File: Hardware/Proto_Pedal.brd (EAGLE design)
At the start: 85.1 x 110.5 mm, 124 parts, among them Q1 2.5A/30V

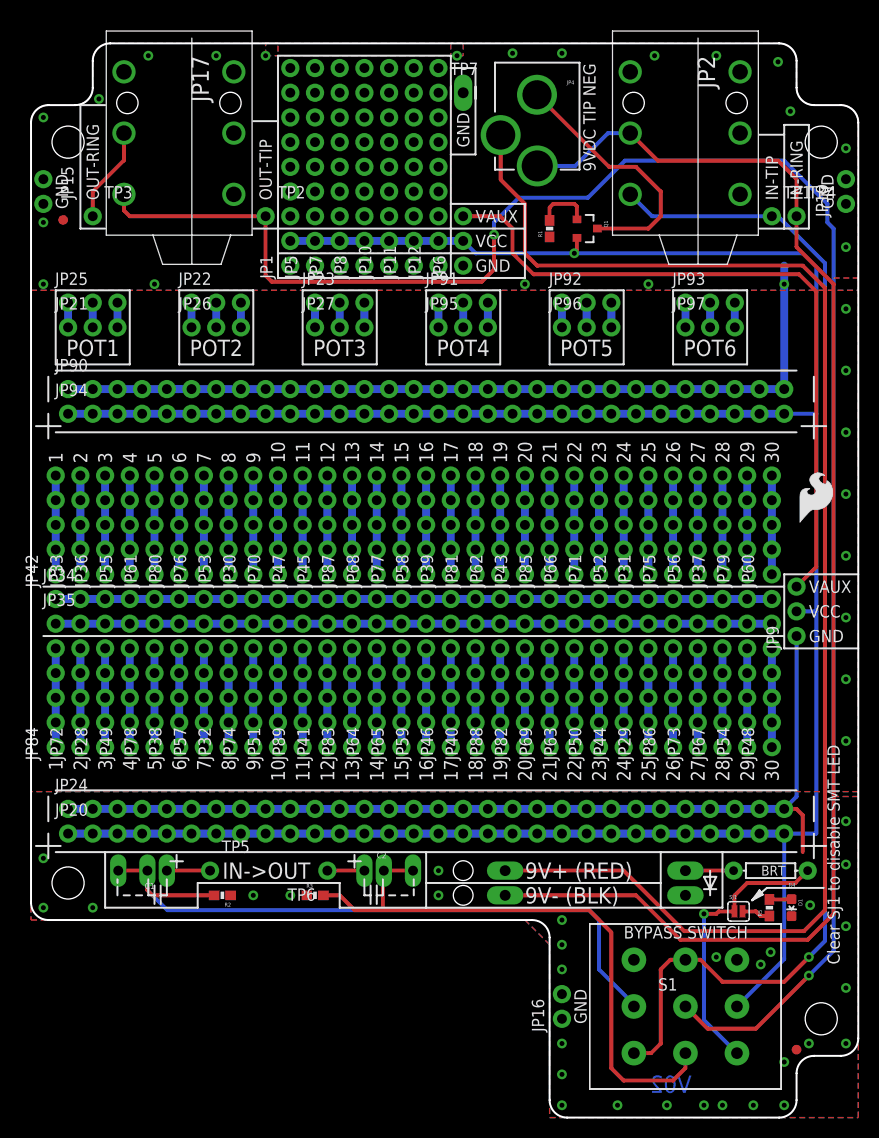
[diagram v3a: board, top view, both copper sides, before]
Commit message: Tweaks from checklist.
- and + signs on rails are a bit smaller.
+'s next to C1 and C2 were overlapping bare copper.
Version bumped to V03.
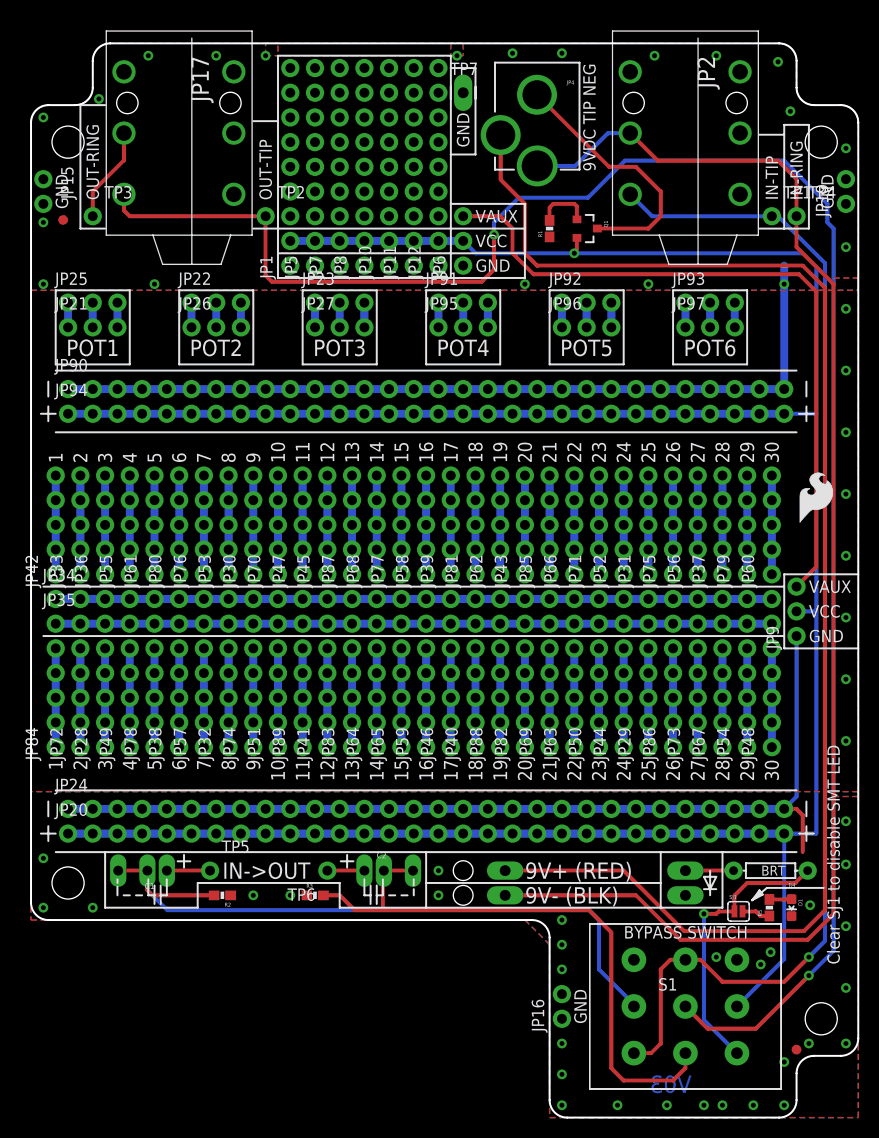
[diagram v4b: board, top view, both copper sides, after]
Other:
- board text added: "V03"
- board text removed: "V02"
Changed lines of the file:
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@@
 <setting verticaltext="up"/>
 </settings>
-<grid distance="0.05" unitdist="inch" unit="inch" style="lines" multiple="1" display="yes" altdistance="0.005" altunitdist="inch" altunit="inch"/>
+<grid distance="0.1" unitdist="inch" unit="inch" style="lines" multiple="1" display="yes" altdistance="0.01" altunitdist="inch" altunit="inch"/>
 <layers>
 <layer number="1" name="Top" color="4" fill="1" visible="yes" active="yes"/>
@@
 <layer number="27" name="tValues" color="7" fill="1" visible="no" active="yes"/>
 <layer number="28" name="bValues" color="7" fill="1" visible="no" active="yes"/>
-<layer number="29" name="tStop" color="7" fill="3" visible="no" active="yes"/>
-<layer number="30" name="bStop" color="7" fill="6" visible="no" active="yes"/>
+<layer number="29" name="tStop" color="7" fill="3" visible="yes" active="yes"/>
+<layer number="30" name="bStop" color="7" fill="6" visible="yes" active="yes"/>
 <layer number="31" name="tCream" color="7" fill="4" visible="no" active="yes"/>
 <layer number="32" name="bCream" color="7" fill="5" visible="no" active="yes"/>
@@
 <wire x1="44.45" y1="17.78" x2="50.8" y2="17.78" width="0.2032" layer="51"/>
 <wire x1="44.45" y1="17.78" x2="44.45" y2="0" width="0.2032" layer="51"/>
-<wire x1="0.508" y1="71.12" x2="1.778" y2="71.12" width="0.2032" layer="21"/>
-<wire x1="1.778" y1="71.12" x2="1.778" y2="69.85" width="0.2032" layer="21"/>
-<wire x1="1.778" y1="72.39" x2="1.778" y2="71.12" width="0.2032" layer="21"/>
-<wire x1="1.778" y1="73.66" x2="1.778" y2="76.2" width="0.2032" layer="21"/>
-<wire x1="0.508" y1="71.12" x2="1.778" y2="71.12" width="0.2032" layer="22"/>
-<wire x1="3.048" y1="71.12" x2="1.778" y2="71.12" width="0.2032" layer="22"/>
-<wire x1="1.778" y1="71.12" x2="1.778" y2="69.85" width="0.2032" layer="22"/>
-<wire x1="1.778" y1="72.39" x2="1.778" y2="71.12" width="0.2032" layer="22"/>
-<wire x1="1.778" y1="73.66" x2="1.778" y2="76.2" width="0.2032" layer="22"/>
-<wire x1="0.508" y1="27.94" x2="1.778" y2="27.94" width="0.2032" layer="21"/>
-<wire x1="3.048" y1="27.94" x2="1.778" y2="27.94" width="0.2032" layer="21"/>
-<wire x1="1.778" y1="27.94" x2="1.778" y2="26.67" width="0.2032" layer="21"/>
-<wire x1="1.778" y1="29.21" x2="1.778" y2="27.94" width="0.2032" layer="21"/>
-<wire x1="1.778" y1="30.48" x2="1.778" y2="33.02" width="0.2032" layer="21"/>
-<wire x1="0.508" y1="27.94" x2="1.778" y2="27.94" width="0.2032" layer="22"/>
-<wire x1="3.048" y1="27.94" x2="1.778" y2="27.94" width="0.2032" layer="22"/>
-<wire x1="1.778" y1="27.94" x2="1.778" y2="26.67" width="0.2032" layer="22"/>
-<wire x1="1.778" y1="29.21" x2="1.778" y2="27.94" width="0.2032" layer="22"/>
-<wire x1="1.778" y1="30.48" x2="1.778" y2="33.02" width="0.2032" layer="22"/>
-<wire x1="79.248" y1="71.12" x2="80.518" y2="71.12" width="0.2032" layer="21"/>
-<wire x1="81.788" y1="71.12" x2="80.518" y2="71.12" width="0.2032" layer="21"/>
-<wire x1="80.518" y1="71.12" x2="80.518" y2="69.85" width="0.2032" layer="21"/>
-<wire x1="80.518" y1="72.39" x2="80.518" y2="71.12" width="0.2032" layer="21"/>
-<wire x1="80.518" y1="73.66" x2="80.518" y2="76.2" width="0.2032" layer="21"/>
-<wire x1="79.248" y1="71.12" x2="80.518" y2="71.12" width="0.2032" layer="22"/>
-<wire x1="81.788" y1="71.12" x2="80.518" y2="71.12" width="0.2032" layer="22"/>
-<wire x1="80.518" y1="71.12" x2="80.518" y2="69.85" width="0.2032" layer="22"/>
-<wire x1="80.518" y1="72.39" x2="80.518" y2="71.12" width="0.2032" layer="22"/>
-<wire x1="80.518" y1="73.66" x2="80.518" y2="76.2" width="0.2032" layer="22"/>
-<wire x1="79.248" y1="27.94" x2="80.518" y2="27.94" width="0.2032" layer="21"/>
-<wire x1="81.788" y1="27.94" x2="80.518" y2="27.94" width="0.2032" layer="21"/>
-<wire x1="80.518" y1="27.94" x2="80.518" y2="26.67" width="0.2032" layer="21"/>
-<wire x1="80.518" y1="29.21" x2="80.518" y2="27.94" width="0.2032" layer="21"/>
-<wire x1="80.518" y1="30.48" x2="80.518" y2="33.02" width="0.2032" layer="21"/>
-<wire x1="79.248" y1="27.94" x2="80.518" y2="27.94" width="0.2032" layer="22"/>
-<wire x1="81.788" y1="27.94" x2="80.518" y2="27.94" width="0.2032" layer="22"/>
-<wire x1="80.518" y1="27.94" x2="80.518" y2="26.67" width="0.2032" layer="22"/>
-<wire x1="80.518" y1="29.21" x2="80.518" y2="27.94" width="0.2032" layer="22"/>
-<wire x1="80.518" y1="30.48" x2="80.518" y2="33.02" width="0.2032" layer="22"/>
 <text x="50.8" y="25.4" size="1.6764" layer="21" font="vector" ratio="15" align="center-left">9V+ (RED)</text>
 <text x="50.8" y="22.86" size="1.6764" layer="21" font="vector" ratio="15" align="center-left">9V- (BLK)</text>
@@
 <text x="69.85" y="80.01" size="1.6764" layer="21" font="vector" ratio="15" align="top-center">POT6</text>
 <wire x1="78.74" y1="70.485" x2="2.54" y2="70.485" width="0.2032" layer="21"/>
-<wire x1="1.778" y1="71.12" x2="3.048" y2="71.12" width="0.2032" layer="21"/>
 <wire x1="78.74" y1="33.655" x2="2.54" y2="33.655" width="0.2032" layer="21"/>
 <wire x1="78.74" y1="27.305" x2="71.12" y2="27.305" width="0.2032" layer="21"/>
@@
 <wire x1="39.37" y1="23.495" x2="39.37" y2="22.86" width="0.2032" layer="21"/>
 <wire x1="39.37" y1="24.511" x2="39.37" y2="23.876" width="0.2032" layer="21"/>
-<wire x1="33.928" y1="26.362" x2="32.62" y2="26.362" width="0.2032" layer="21"/>
-<wire x1="33.274" y1="27.016" x2="33.274" y2="25.708" width="0.2032" layer="21"/>
+<wire x1="33.166" y1="26.362" x2="31.858" y2="26.362" width="0.2032" layer="21"/>
+<wire x1="32.512" y1="27.016" x2="32.512" y2="25.708" width="0.2032" layer="21"/>
 <wire x1="40.64" y1="27.305" x2="40.64" y2="24.13" width="0.2032" layer="22"/>
 <wire x1="40.64" y1="21.59" x2="31.75" y2="21.59" width="0.2032" layer="22"/>
@@
 <wire x1="8.89" y1="23.749" x2="8.89" y2="22.86" width="0.2032" layer="22"/>
 <wire x1="8.89" y1="24.511" x2="8.89" y2="24.13" width="0.2032" layer="22"/>
-<wire x1="32.62" y1="26.362" x2="33.928" y2="26.362" width="0.2032" layer="22"/>
-<wire x1="33.274" y1="27.016" x2="33.274" y2="25.708" width="0.2032" layer="22"/>
+<wire x1="31.858" y1="26.362" x2="33.166" y2="26.362" width="0.2032" layer="22"/>
+<wire x1="32.512" y1="27.016" x2="32.512" y2="25.708" width="0.2032" layer="22"/>
 <text x="19.177" y="25.4" size="1.6764" layer="22" font="vector" ratio="15" rot="MR180" align="center-left">OUT&lt;-IN</text>
-<text x="67.945" y="2.54" size="1.778" layer="16" font="vector" ratio="15" rot="MR0">V02</text>
+<text x="67.945" y="2.54" size="1.778" layer="16" font="vector" ratio="15" rot="MR0">V03</text>
 <dimension x1="0" y1="0" x2="0" y2="110.49" x3="-16.51" y3="55.245" textsize="1.778" textratio="15" layer="47" unit="inch"/>
 <text x="11.43" y="-19.05" size="2.54" layer="47" ratio="15">All Dimensions in inches
@@
 <wire x1="80.01" y1="91.44" x2="80.01" y2="102.108" width="0.2032" layer="21"/>
 <text x="78.74" y="94.361" size="1.27" layer="22" font="vector" ratio="15" rot="MR90" align="center-left">IN-RING</text>
-<wire x1="15.628" y1="26.362" x2="14.32" y2="26.362" width="0.2032" layer="21"/>
-<wire x1="14.974" y1="27.016" x2="14.974" y2="25.708" width="0.2032" layer="21"/>
-<wire x1="14.32" y1="26.362" x2="15.628" y2="26.362" width="0.2032" layer="22"/>
-<wire x1="14.974" y1="27.016" x2="14.974" y2="25.708" width="0.2032" layer="22"/>
+<wire x1="16.39" y1="26.362" x2="15.082" y2="26.362" width="0.2032" layer="21"/>
+<wire x1="15.736" y1="27.016" x2="15.736" y2="25.708" width="0.2032" layer="21"/>
+<wire x1="15.082" y1="26.362" x2="16.39" y2="26.362" width="0.2032" layer="22"/>
+<wire x1="15.736" y1="27.016" x2="15.736" y2="25.708" width="0.2032" layer="22"/>
 <dimension x1="0" y1="110.49" x2="52.07" y2="110.49" x3="26.035" y3="138.684" textsize="2.54" textratio="15" layer="47" unit="inch"/>
 <text x="2.54" y="95.25" size="1.27" layer="22" font="vector" ratio="15" rot="MR270" align="top-center">GND</text>
@@
 <wire x1="74.7268" y1="22.987" x2="74.93" y2="23.1648" width="0.254" layer="21"/>
 <wire x1="74.93" y1="23.1648" x2="75.0316" y2="22.987" width="0.254" layer="21"/>
+<wire x1="79.756" y1="32.512" x2="79.756" y2="30.988" width="0.2032" layer="21"/>
+<wire x1="79.756" y1="29.972" x2="79.756" y2="28.448" width="0.2032" layer="21"/>
+<wire x1="78.994" y1="29.21" x2="80.518" y2="29.21" width="0.2032" layer="21"/>
+<wire x1="79.756" y1="32.512" x2="79.756" y2="30.988" width="0.2032" layer="22"/>
+<wire x1="79.756" y1="29.972" x2="79.756" y2="28.448" width="0.2032" layer="22"/>
+<wire x1="80.518" y1="29.21" x2="78.994" y2="29.21" width="0.2032" layer="22"/>
+<wire x1="1.778" y1="32.512" x2="1.778" y2="30.988" width="0.2032" layer="21"/>
+<wire x1="1.778" y1="29.972" x2="1.778" y2="28.448" width="0.2032" layer="21"/>
+<wire x1="1.016" y1="29.21" x2="2.54" y2="29.21" width="0.2032" layer="21"/>
+<wire x1="1.778" y1="32.512" x2="1.778" y2="30.988" width="0.2032" layer="22"/>
+<wire x1="1.778" y1="29.972" x2="1.778" y2="28.448" width="0.2032" layer="22"/>
+<wire x1="2.54" y1="29.21" x2="1.016" y2="29.21" width="0.2032" layer="22"/>
+<wire x1="1.778" y1="75.692" x2="1.778" y2="74.168" width="0.2032" layer="21"/>
+<wire x1="1.778" y1="73.152" x2="1.778" y2="71.628" width="0.2032" layer="21"/>
+<wire x1="1.016" y1="72.39" x2="2.54" y2="72.39" width="0.2032" layer="21"/>
+<wire x1="1.778" y1="75.692" x2="1.778" y2="74.168" width="0.2032" layer="22"/>
+<wire x1="1.778" y1="73.152" x2="1.778" y2="71.628" width="0.2032" layer="22"/>
+<wire x1="2.54" y1="72.39" x2="1.016" y2="72.39" width="0.2032" layer="22"/>
+<wire x1="79.756" y1="75.692" x2="79.756" y2="74.168" width="0.2032" layer="21"/>
+<wire x1="79.756" y1="73.152" x2="79.756" y2="71.628" width="0.2032" layer="21"/>
+<wire x1="78.994" y1="72.39" x2="80.518" y2="72.39" width="0.2032" layer="21"/>
+<wire x1="79.756" y1="75.692" x2="79.756" y2="74.168" width="0.2032" layer="22"/>
+<wire x1="79.756" y1="73.152" x2="79.756" y2="71.628" width="0.2032" layer="22"/>
+<wire x1="80.518" y1="72.39" x2="78.994" y2="72.39" width="0.2032" layer="22"/>
 </plain>
 <attributes>
